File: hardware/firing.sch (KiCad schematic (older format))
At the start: 60 parts

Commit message: Firing matrix and CC SMPS
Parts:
- added C301: 22u, agg:1206, symbol C
- added C302: 10n, agg:0805, symbol C
- added C303, C304: 100n, agg:0603, symbol C
- added C305: 4u7, agg:0603, symbol C
- added D301, D302: PMEG2005AEA, agg:SOD-323, symbol SCHOTTKY
- added D303: SS110B, agg:DO-214AA-SMB, symbol D_Schottky
- added D304: STPS3L40UF, agg:DO-214AA-SMB, symbol D_Schottky
- added IC301: TPS92512, agg:MSOP-10-EP-TI, symbol TPS92512
- added L301: 12uH, hardware:SRR1260A, symbol INDUCTOR
- added R301: 30k, agg:0603, symbol R
- added R302: 10k, agg:0603, symbol R
- added R303: 10M, agg:0603, symbol R
- added R304, R306: 3k3, agg:0603, symbol R
- added R305: 200k, agg:0603, symbol R
- added R307: 1k, agg:0603, symbol R
- added R308: 0R15 1W, 2512, symbol R
- gave numbers to parts that had none: 60
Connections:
- net +6V: now also C301.1, D303.1 (K), IC301.2 (VIN), R301.1, R303.2
- net ARM: now also IC301.4 (PDIM)
- net BUS: now also C305.1, D303.2 (A), L301.1, R304.1, R306.2
- net CONT: now also D302.2, R306.1
- net CONT_EN: now also D301.2, R304.2
- net GND: now also C301.2, C302.2, C303.2, D304.2 (A), IC301.9 (GND), IC301.EP (GND), R302.2, R305.2, R308.2; no longer Q301.2 (S), Q302.2 (S), Q303.2 (S), Q304.2 (S), Q305.2 (S), Q306.2 (S), Q307.2 (S), Q308.2 (S), Q309.2 (S), Q310.2 (S), Q311.2 (S), Q312.2 (S), Q313.2 (S), Q314.2 (S), Q315.2 (S), Q316.2 (S), Q317.2 (S), Q318.2 (S), Q319.2 (S), Q320.2 (S), Q321.2 (S), Q322.2 (S), Q323.2 (S), Q324.2 (S), Q325.2 (S), Q326.2 (S), Q327.2 (S), Q328.2 (S), Q329.2 (S), Q330.2 (S)
- new net: C304.1, IC301.1 (BOOT)
- new net: C304.2, D304.1 (K), IC301.10 (PH), L301.2
- new net: IC301.3 (UVLO), R301.2, R302.1
- new net: IC301.5 (RT/CLK), R305.1
- new net: C302.1, IC301.6 (IADJ), R303.1
- new net: IC301.7 (ISENSE), R307.2
- new net: C303.1, IC301.8 (COMP)
- new net 3v3: D301.1, D302.1
- new net RETURN: C305.2, Q301.2 (S), Q302.2 (S), Q303.2 (S), Q304.2 (S), Q305.2 (S), Q306.2 (S), Q307.2 (S), Q308.2 (S), Q309.2 (S), Q310.2 (S), Q311.2 (S), Q312.2 (S), Q313.2 (S), Q314.2 (S), Q315.2 (S), Q316.2 (S), Q317.2 (S), Q318.2 (S), Q319.2 (S), Q320.2 (S), Q321.2 (S), Q322.2 (S), Q323.2 (S), Q324.2 (S), Q325.2 (S), Q326.2 (S), Q327.2 (S), Q328.2 (S), Q329.2 (S), Q330.2 (S), R307.1, R308.1
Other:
- note added: "Schottkys clamp firing voltage\nto 3v3 to protect inputs\n3k3 sets cont current\nto 3.3V / 3.3kR = 1mA\nand limits clamp current\nto (12-3.3)V / 3.3kR = 3mA"

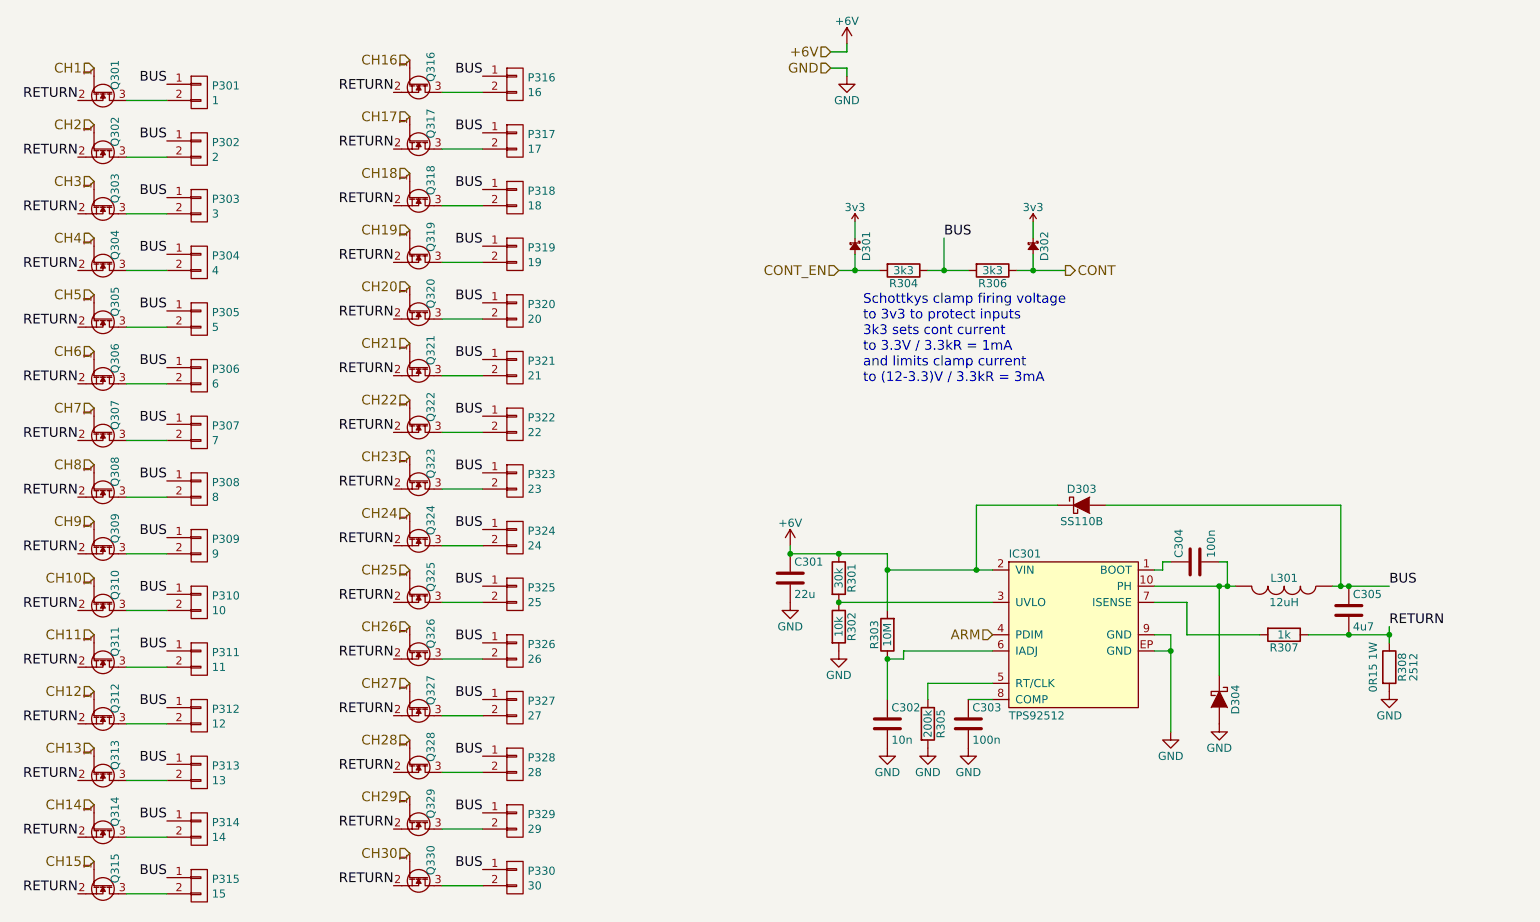
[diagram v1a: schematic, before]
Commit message: aux power, test points
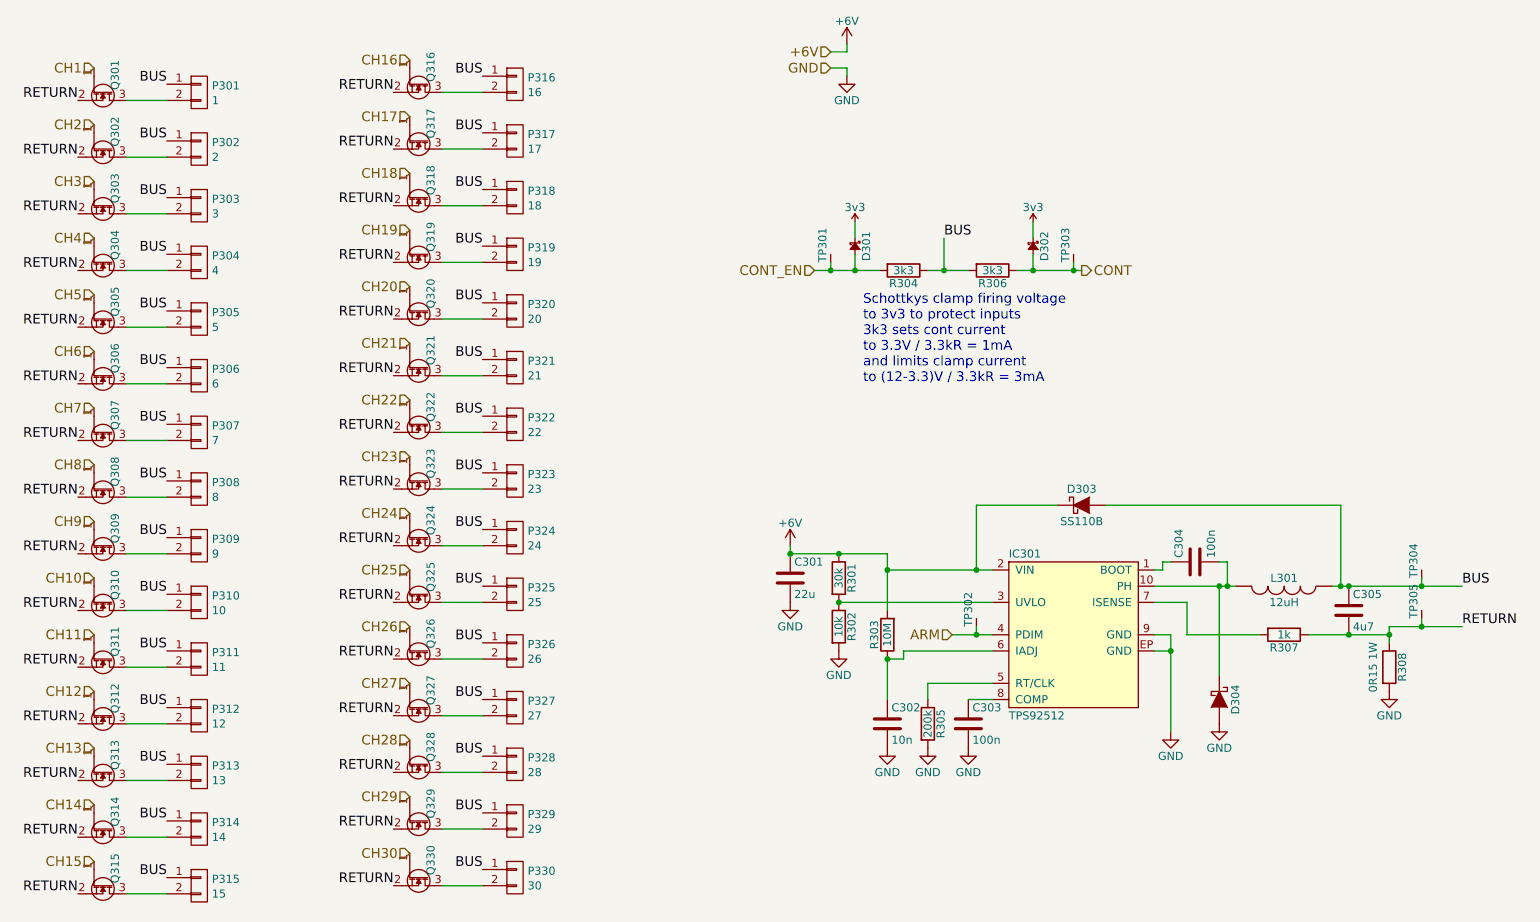
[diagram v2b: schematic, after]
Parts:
- added TP301: CONT_EN, agg:TESTPAD, symbol TESTPAD
- added TP302: ARM, agg:TESTPAD, symbol TESTPAD
- added TP303: CONT_MEAS, agg:TESTPAD, symbol TESTPAD
- added TP304: BUS, hardware:Test_point_mini, symbol TESTPAD
- added TP305: RETURN, hardware:Test_point_mini, symbol TESTPAD
- P301, P302, P303, P304, P305, P306, P307, P308, P309, P310, P311, P312, P313, P314, P315, P316, P317, P318, P319, P320, P321, P322, P323, P324, P325, P326, P327, P328, P329, P330: Farnell (none) -> 1792951
- R308: footprint 2512 -> agg:2512
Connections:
- net ARM: now also TP302.1 (TP)
- net BUS: now also TP304.1 (TP)
- net CONT: now also TP303.1 (TP)
- net CONT_EN: now also TP301.1 (TP)
- net RETURN: now also TP305.1 (TP)
